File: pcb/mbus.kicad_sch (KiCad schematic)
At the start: 25 parts, among them Q2 BC846, Q3 BSS84, Q4 BC846, U3 MC33072, U4 LM4040DBZ-5

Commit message: * Work in progress
  - Add generate script
  - Add switch model
  - Start routing
  - Tidy schematic
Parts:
- added R31: 20K, Resistor_SMD:R_0402_1005Metric, symbol Device:R
- added R32: 1K, Resistor_SMD:R_0402_1005Metric, symbol Device:R
- C3: Voltage (none) -> 50V
- R9: MPN (none) -> ERJ-P06J101V; Manufacturer (none) -> Panasonic; Mouser (none) -> 667-ERJ-P06J101V; Power (none) -> 0.5W
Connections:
- net GND: now also R32.2
- net DIFF_5X renamed DIFF_5V
- net DIFF_5V: now also R31.1
- new net MBUS_OC: R31.2, R32.1
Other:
- note added: "(V > 5) saturates at 0V"
- note removed: "(V > 5) > pull low"
- note removed: "Rate for 30 mA (~90 mW)"
- note removed: "Reduce common mode voltage range to (V_{CC} - 2V7)."
- title: MBUS Master Prototype -> emonHP
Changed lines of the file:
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@@
   (paper "A4")
   (title_block
-    (title "MBUS Master Prototype")
-    (date "2024-06-26")
+    (title "emonHP")
+    (date "2024-07-02")
     (rev "0")
     (company "Tilt Ltd / OpenEnergyMonitor")
@@
   (junction (at 140.97 101.6) (diameter 0) (color 0 0 0 0)
   )
-  (junction (at 161.29 99.06) (diameter 0) (color 0 0 0 0)
-  )
   (junction (at 116.84 92.71) (diameter 0) (color 0 0 0 0)
   )
+  (junction (at 220.98 46.99) (diameter 0) (color 0 0 0 0)
+  )
   (junction (at 181.61 63.5) (diameter 0) (color 0 0 0 0)
   )
@@
     (stroke (width 0) (type default))
   )
+  (wire (pts (xy 220.98 44.45) (xy 220.98 46.99))
+    (stroke (width 0) (type default))
+  )
   (wire (pts (xy 135.89 96.52) (xy 135.89 107.95))
     (stroke (width 0) (type default))
@@
     (stroke (width 0) (type default))
   )
+  (wire (pts (xy 220.98 57.15) (xy 220.98 59.69))
+    (stroke (width 0) (type default))
+  )
   (wire (pts (xy 161.29 119.38) (xy 161.29 133.35))
     (stroke (width 0) (type default))
@@
     (stroke (width 0) (type default))
   )
-  (wire (pts (xy 161.29 99.06) (xy 171.45 99.06))
-    (stroke (width 0) (type default))
-  )
   (wire (pts (xy 54.61 57.15) (xy 68.58 57.15))
     (stroke (width 0) (type default))
@@
     (stroke (width 0) (type default))
   )
+  (wire (pts (xy 220.98 34.29) (xy 220.98 36.83))
+    (stroke (width 0) (type default))
+  )
   (wire (pts (xy 218.44 95.25) (xy 218.44 97.79))
     (stroke (width 0) (type default))
@@
     (stroke (width 0) (type default))
   )
+  (wire (pts (xy 220.98 46.99) (xy 220.98 49.53))
+    (stroke (width 0) (type default))
+  )
   (wire (pts (xy 22.86 80.01) (xy 34.29 80.01))
     (stroke (width 0) (type default))
@@
     (stroke (width 0) (type default))
   )
+  (wire (pts (xy 220.98 46.99) (xy 233.68 46.99))
+    (stroke (width 0) (type default))
+  )
   (wire (pts (xy 120.65 92.71) (xy 116.84 92.71))
     (stroke (width 0) (type default))
@@
     (stroke (width 0) (type default))
   )
-  (text "Rate for 30 mA (~90 mW)" (at 73.66 100.33 0)
-    (effects (font (size 1.27 1.27)) (justify left bottom))
-  )
-  (text "Reduce common mode voltage\nrange to (V_{CC} - 2V7)."
-    (at 73.66 86.36 0)
-    (effects (font (size 1.27 1.27)) (justify left bottom))
+  (text_box "When the voltage through the shunt resistor is >5 V, this indicates a short on MBUS, so shut down."
+    (at 237.49 30.48 0) (size 29.21 10.16)
+    (stroke (width 0) (type default))
+    (fill (type none))
+    (effects (font (size 1.27 1.27)) (justify left top))
+  )
+  (text_box "Reduce common mode voltage\nrange to (V_{CC} - 2V7)."
+    (at 68.58 81.28 0) (size 33.02 6.35)
+    (stroke (width 0) (type default))
+    (fill (type none))
+    (effects (font (size 1.27 1.27)) (justify left top))
   )
   (text "Gain: 5" (at 134.62 92.71 0)
     (effects (font (size 1.27 1.27)) (justify left bottom))
   )
-  (text "(V > 5) > pull low" (at 193.04 123.19 0)
+  (text "(V > 5) saturates at 0V" (at 184.15 124.46 0)
     (effects (font (size 1.27 1.27)) (justify left bottom))
   )
@@
     (effects (font (size 1.27 1.27)) (justify right bottom))
   )
-  (label "V_{Z}" (at 132.08 76.2 180) (fields_autoplaced)
-    (effects (font (size 1.27 1.27)) (justify right bottom))
-  )
   (label "MBUS_A" (at 109.22 132.08 0) (fields_autoplaced)
     (effects (font (size 1.27 1.27)) (justify left bottom))
   )
+  (label "DIFF_5V" (at 220.98 34.29 0) (fields_autoplaced)
+    (effects (font (size 1.27 1.27)) (justify left bottom))
+  )
   (label "36V" (at 54.61 57.15 0) (fields_autoplaced)
     (effects (font (size 1.27 1.27)) (justify left bottom))
@@
     (effects (font (size 1.27 1.27)) (justify right bottom))
   )
+  (label "DIFF_5V" (at 161.29 99.06 0) (fields_autoplaced)
+    (effects (font (size 1.27 1.27)) (justify left bottom))
+  )
   (hierarchical_label "MBUS_A" (shape output) (at 100.33 132.08 180) (fields_autoplaced)
     (effects (font (size 1.27 1.27)) (justify right))
@@
     (effects (font (size 1.27 1.27)) (justify left))
   )
-  (hierarchical_label "DIFF_5X" (shape output) (at 171.45 99.06 0) (fields_autoplaced)
+  (hierarchical_label "MBUS_OC" (shape passive) (at 233.68 46.99 0) (fields_autoplaced)
     (effects (font (size 1.27 1.27)) (justify left))
   )
@@
     )
   )
+  (symbol (lib_id "power:GND") (at 220.98 59.69 0) (unit 1)
+    (in_bom yes) (on_board yes) (dnp no) (fields_autoplaced)
+    (property "Reference" "#PWR052" (at 220.98 66.04 0)
+      (effects (font (size 1.27 1.27)) hide)
+    )
+    (property "Value" "GND" (at 220.98 64.77 0)
+      (effects (font (size 1.27 1.27)))
+    )
+    (property "Footprint" "" (at 220.98 59.69 0)
+      (effects (font (size 1.27 1.27)) hide)
+    )
+    (property "Datasheet" "" (at 220.98 59.69 0)
+      (effects (font (size 1.27 1.27)) hide)
+    )
+    (pin "1")
+    (instances
+      (project "emonHP"
+        (path "/afefbb79-c2cc-4097-b792-3e37a295b6e5"
+          (reference "#PWR052") (unit 1)
+        )
+        (path "/afefbb79-c2cc-4097-b792-3e37a295b6e5/47d3f211-4a48-4ab2-adbe-56046b34137e"
+          (reference "#PWR052") (unit 1)
+        )
+      )
+    )
+  )
   (symbol (lib_id "Device:R") (at 34.29 71.12 180) (unit 1)
     (in_bom yes) (on_board yes) (dnp no) (fields_autoplaced)
@@
   )
   (symbol (lib_id "Device:C") (at 194.31 71.12 0) (mirror y) (unit 1)
-    (in_bom yes) (on_board yes) (dnp no) (fields_autoplaced)
+    (in_bom yes) (on_board yes) (dnp no)
     (property "Reference" "C3" (at 190.5 70.485 0)
       (effects (font (size 1.27 1.27)) (justify left))
@@
       (effects (font (size 1.27 1.27)) hide)
     )
+    (property "Voltage" "50V" (at 189.23 76.2 0)
+      (effects (font (size 1.27 1.27)))
+    )
     (pin "1")
     (pin "2")
@@
   )
   (symbol (lib_id "Device:R") (at 116.84 99.06 0) (mirror y) (unit 1)
-    (in_bom yes) (on_board yes) (dnp no) (fields_autoplaced)
+    (in_bom yes) (on_board yes) (dnp no)
     (property "Reference" "R9" (at 114.3 98.425 0)
       (effects (font (size 1.27 1.27)) (justify left))
@@
       (effects (font (size 1.27 1.27)) hide)
     )
+    (property "Manufacturer" "Panasonic" (at 116.84 99.06 0)
+      (effects (font (size 1.27 1.27)) hide)
+    )
+    (property "MPN" "ERJ-P06J101V" (at 116.84 99.06 0)
+      (effects (font (size 1.27 1.27)) hide)
+    )
+    (property "Mouser" "667-ERJ-P06J101V" (at 116.84 99.06 0)
+      (effects (font (size 1.27 1.27)) hide)
+    )
+    (property "Power" "0.5W" (at 111.76 102.87 0)
+      (effects (font (size 1.27 1.27)))
+    )
     (pin "1")
     (pin "2")
@@
         )
       )
+    )
+  )
+  (symbol (lib_id "Device:R") (at 220.98 40.64 0) (unit 1)
+    (in_bom yes) (on_board yes) (dnp no) (fields_autoplaced)
+    (property "Reference" "R31" (at 223.52 40.005 0)
+      (effects (font (size 1.27 1.27)) (justify left))
+    )
+    (property "Value" "20K" (at 223.52 42.545 0)
+      (effects (font (size 1.27 1.27)) (justify left))
+    )
+    (property "Footprint" "Resistor_SMD:R_0402_1005Metric" (at 219.202 40.64 90)
+      (effects (font (size 1.27 1.27)) hide)
+    )
+    (property "Datasheet" "~" (at 220.98 40.64 0)
+      (effects (font (size 1.27 1.27)) hide)
+    )
+    (pin "1")
+    (pin "2")
+    (instances
+      (project "emonHP"
+        (path "/afefbb79-c2cc-4097-b792-3e37a295b6e5"
+          (reference "R31") (unit 1)
+        )
+        (path "/afefbb79-c2cc-4097-b792-3e37a295b6e5/47d3f211-4a48-4ab2-adbe-56046b34137e"
+          (reference "R31") (unit 1)
+        )
+      )
+    )
+  )
+  (symbol (lib_id "Device:R") (at 220.98 53.34 0) (unit 1)
+    (in_bom yes) (on_board yes) (dnp no) (fields_autoplaced)
+    (property "Reference" "R32" (at 223.52 52.705 0)
+      (effects (font (size 1.27 1.27)) (justify left))
+    )
+    (property "Value" "1K" (at 223.52 55.245 0)
+      (effects (font (size 1.27 1.27)) (justify left))
+    )
+    (property "Footprint" "Resistor_SMD:R_0402_1005Metric" (at 219.202 53.34 90)
+      (effects (font (size 1.27 1.27)) hide)
+    )
+    (property "Datasheet" "~" (at 220.98 53.34 0)
+      (effects (font (size 1.27 1.27)) hide)
+    )
+    (pin "1")
+    (pin "2")
+    (instances
+      (project "emonHP"
+        (path "/afefbb79-c2cc-4097-b792-3e37a295b6e5"
+          (reference "R32") (unit 1)
+        )
+        (path "/afefbb79-c2cc-4097-b792-3e37a295b6e5/47d3f211-4a48-4ab2-adbe-56046b34137e"
+          (reference "R32") (unit 1)
+        )
+      )

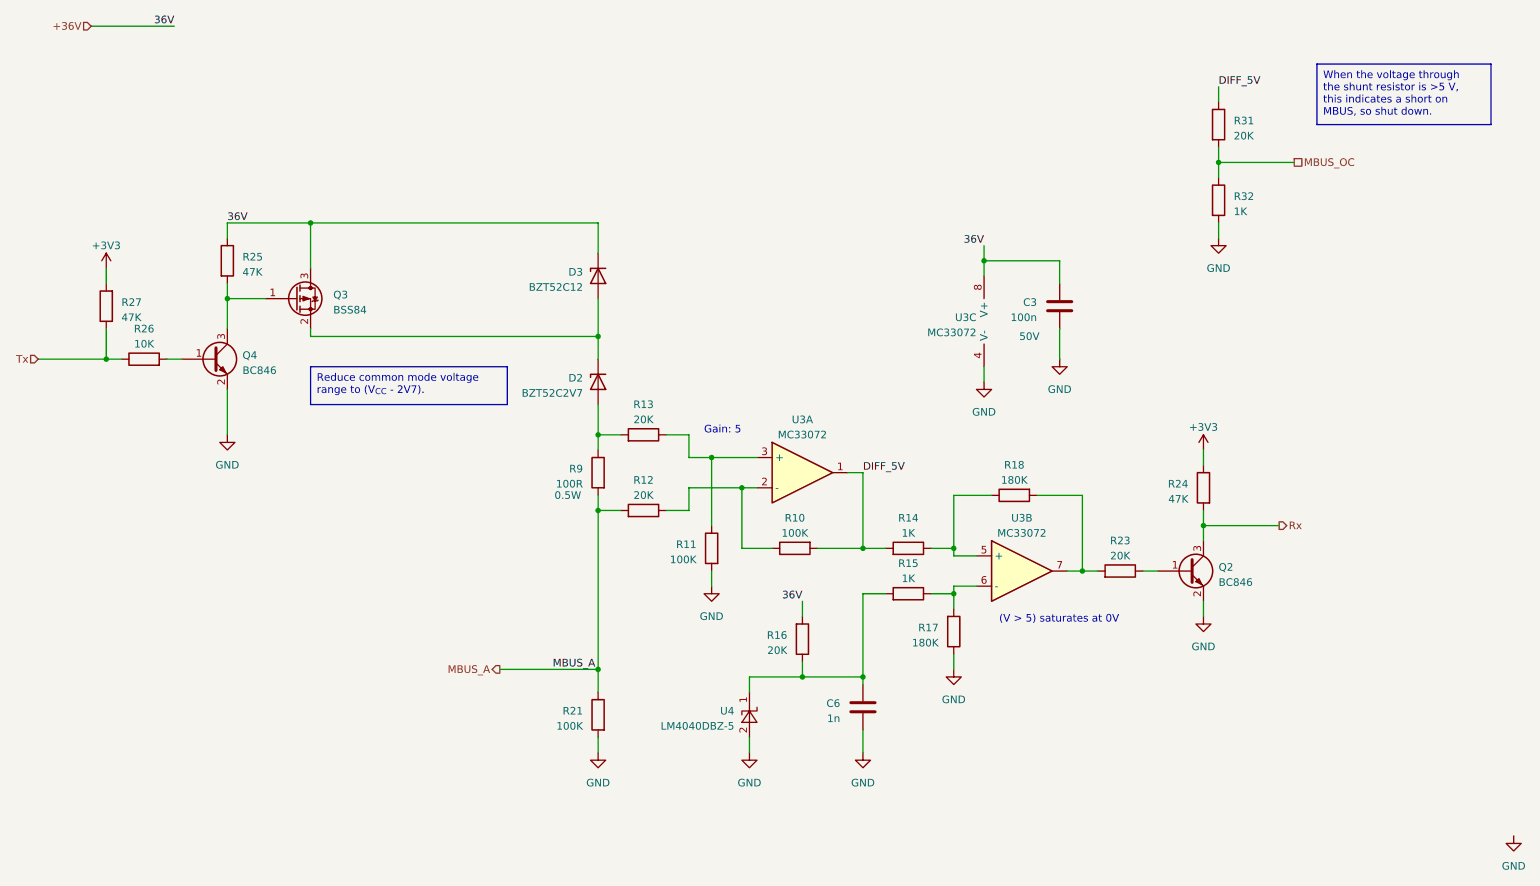
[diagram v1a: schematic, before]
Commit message: * [0.1-dev] Voltage good
  - Add 36V voltage good detection
  - Add all 3D models
  - Correct footprint for front LED
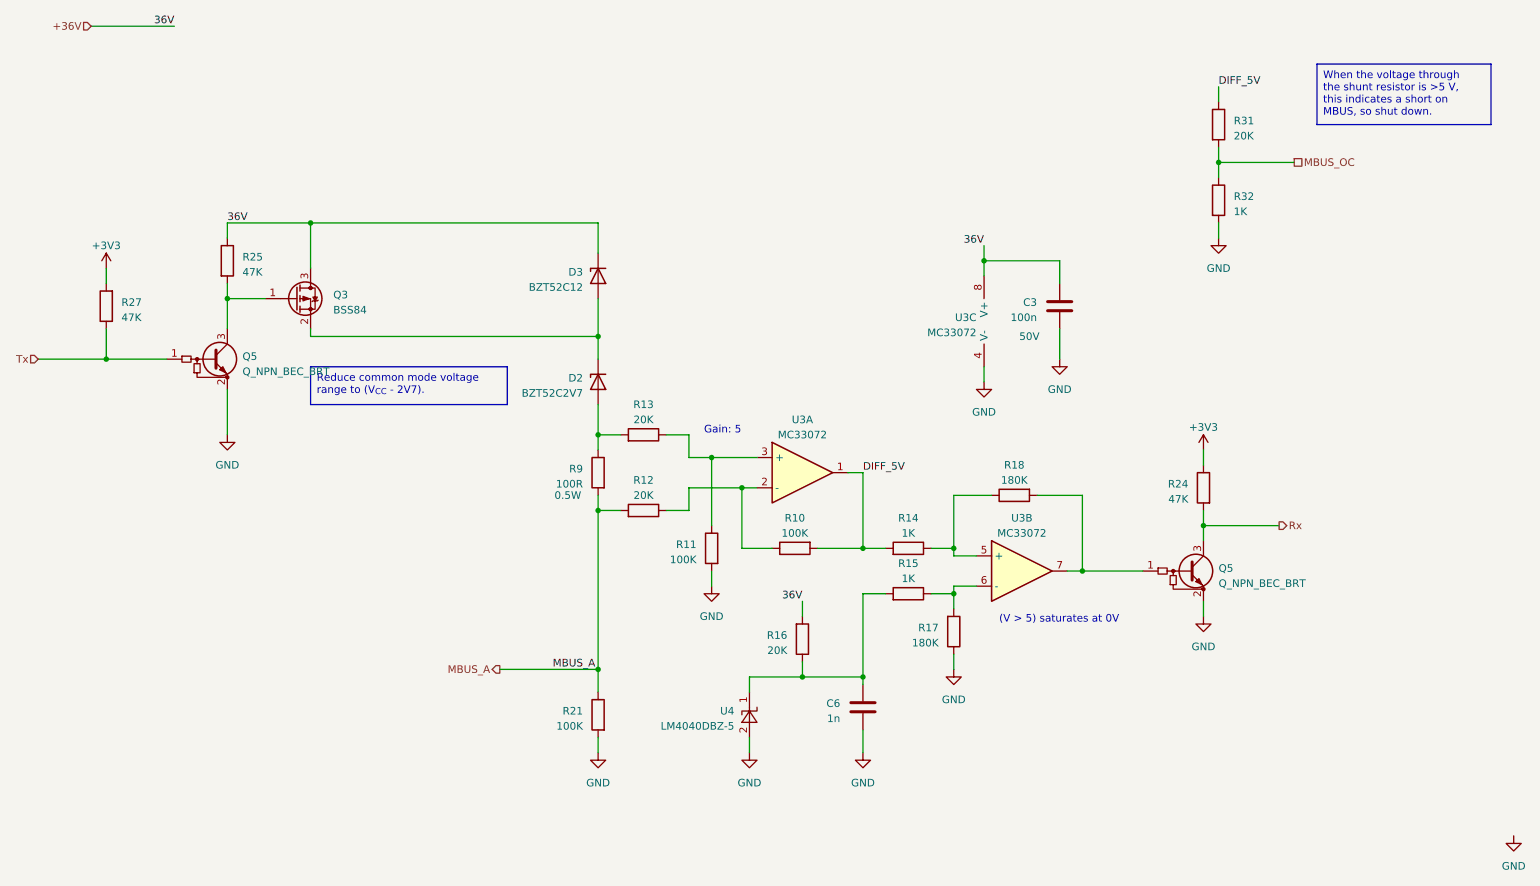
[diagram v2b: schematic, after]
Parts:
- removed Q2, Q4: BC846, Package_TO_SOT_SMD:SOT-23, symbol Transistor_BJT:BC846
- removed R23: 20K, Resistor_SMD:R_0402_1005Metric, symbol Device:R
- removed R26: 10K, Resistor_SMD:R_0402_1005Metric, symbol Device:R
- added Q5 (x2): Q_NPN_BEC_BRT, Package_TO_SOT_SMD:SOT-23, symbol Device:Q_NPN_BEC_BRT
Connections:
- net GND: now also Q5.2 (E), Q5.2 (E)
- net Rx: now also Q5.3 (C)
- net Tx: now also Q5.1 (B)
- net at Q3.1 (G), R25.2: now also Q5.3 (C)
- net at R18.2, U3.7: now also Q5.1 (B)
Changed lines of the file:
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@@
     (stroke (width 0) (type default))
   )
-  (wire (pts (xy 36.83 80.01) (xy 34.29 80.01))
+  (wire (pts (xy 34.29 80.01) (xy 44.45 80.01))
     (stroke (width 0) (type default))
   )
@@
     (stroke (width 0) (type default))
   )
-  (wire (pts (xy 44.45 80.01) (xy 46.99 80.01))
-    (stroke (width 0) (type default))
-  )
   (wire (pts (xy 231.14 107.95) (xy 218.44 107.95))
     (stroke (width 0) (type default))
@@
     (stroke (width 0) (type default))
   )
-  (wire (pts (xy 210.82 115.57) (xy 208.28 115.57))
-    (stroke (width 0) (type default))
-  )
   (wire (pts (xy 116.84 92.71) (xy 116.84 95.25))
     (stroke (width 0) (type default))
@@
     (stroke (width 0) (type default))
   )
-  (wire (pts (xy 200.66 115.57) (xy 198.12 115.57))
+  (wire (pts (xy 198.12 115.57) (xy 208.28 115.57))
     (stroke (width 0) (type default))
   )
@@
     )
   )
+  (symbol (lib_id "Device:Q_NPN_BEC_BRT") (at 53.34 80.01 0) (unit 1)
+    (in_bom yes) (on_board yes) (dnp no) (fields_autoplaced)
+    (property "Reference" "Q5" (at 57.15 79.5528 0)
+      (effects (font (size 1.27 1.27)) (justify left))
+    )
+    (property "Value" "Q_NPN_BEC_BRT" (at 57.15 82.0928 0)
+      (effects (font (size 1.27 1.27)) (justify left))
+    )
+    (property "Footprint" "Package_TO_SOT_SMD:SOT-23" (at 53.34 80.01 0)
+      (effects (font (size 1.27 1.27)) hide)
+    )
+    (property "Datasheet" "~" (at 53.34 80.01 0)
+      (effects (font (size 1.27 1.27)) hide)
+    )
+    (pin "1")
+    (pin "2")
+    (pin "3")
+    (instances
+      (project "emonHP"
+        (path "/afefbb79-c2cc-4097-b792-3e37a295b6e5"
+          (reference "Q5") (unit 1)
+        )
+        (path "/afefbb79-c2cc-4097-b792-3e37a295b6e5/47d3f211-4a48-4ab2-adbe-56046b34137e"
+          (reference "Q1") (unit 1)
+        )
+      )
+    )
+  )
   (symbol (lib_id "power:GND") (at 142.24 146.05 0) (mirror y) (unit 1)
     (in_bom yes) (on_board yes) (dnp no) (fields_autoplaced)
@@
         (path "/afefbb79-c2cc-4097-b792-3e37a295b6e5/47d3f211-4a48-4ab2-adbe-56046b34137e"
           (reference "R10") (unit 1)
-        )
-      )
-    )
-  )
-  (symbol (lib_id "Transistor_BJT:BC846") (at 52.07 80.01 0) (unit 1)
-    (in_bom yes) (on_board yes) (dnp no) (fields_autoplaced)
-    (property "Reference" "Q4" (at 57.15 79.375 0)
-      (effects (font (size 1.27 1.27)) (justify left))
-    )
-    (property "Value" "BC846" (at 57.15 81.915 0)
-      (effects (font (size 1.27 1.27)) (justify left))
-    )
-    (property "Footprint" "Package_TO_SOT_SMD:SOT-23" (at 57.15 81.915 0)
-      (effects (font (size 1.27 1.27) italic) (justify left) hide)
-    )
-    (property "Datasheet" "https://assets.nexperia.com/documents/data-sheet/BC846_SER.pdf" (at 52.07 80.01 0)
-      (effects (font (size 1.27 1.27)) (justify left) hide)
-    )
-    (pin "1")
-    (pin "2")
-    (pin "3")
-    (instances
-      (project "mbus-reader-proto"
-        (path "/36d146b0-f348-4341-a935-471af0e684a6"
-          (reference "Q4") (unit 1)
-        )
-      )
-      (project "emonHP"
-        (path "/afefbb79-c2cc-4097-b792-3e37a295b6e5/47d3f211-4a48-4ab2-adbe-56046b34137e"
-          (reference "Q1") (unit 1)
         )
       )
@@
     )
   )
-  (symbol (lib_id "Device:R") (at 204.47 115.57 270) (mirror x) (unit 1)
-    (in_bom yes) (on_board yes) (dnp no) (fields_autoplaced)
-    (property "Reference" "R23" (at 204.47 110.49 90)
-      (effects (font (size 1.27 1.27)))
-    )
-    (property "Value" "20K" (at 204.47 113.03 90)
-      (effects (font (size 1.27 1.27)))
-    )
-    (property "Footprint" "Resistor_SMD:R_0402_1005Metric" (at 204.47 117.348 90)
-      (effects (font (size 1.27 1.27)) hide)
-    )
-    (property "Datasheet" "~" (at 204.47 115.57 0)
-      (effects (font (size 1.27 1.27)) hide)
-    )
-    (pin "1")
-    (pin "2")
-    (instances
-      (project "mbus-reader-proto"
-        (path "/36d146b0-f348-4341-a935-471af0e684a6"
-          (reference "R23") (unit 1)
-        )
-      )
-      (project "emonHP"
-        (path "/afefbb79-c2cc-4097-b792-3e37a295b6e5/47d3f211-4a48-4ab2-adbe-56046b34137e"
-          (reference "R25") (unit 1)
-        )
-      )
-    )
-  )
-  (symbol (lib_id "Device:R") (at 40.64 80.01 90) (unit 1)
-    (in_bom yes) (on_board yes) (dnp no) (fields_autoplaced)
-    (property "Reference" "R26" (at 40.64 74.93 90)
-      (effects (font (size 1.27 1.27)))
-    )
-    (property "Value" "10K" (at 40.64 77.47 90)
-      (effects (font (size 1.27 1.27)))
-    )
-    (property "Footprint" "Resistor_SMD:R_0402_1005Metric" (at 40.64 81.788 90)
-      (effects (font (size 1.27 1.27)) hide)
-    )
-    (property "Datasheet" "~" (at 40.64 80.01 0)
-      (effects (font (size 1.27 1.27)) hide)
-    )
-    (pin "1")
-    (pin "2")
-    (instances
-      (project "mbus-reader-proto"
-        (path "/36d146b0-f348-4341-a935-471af0e684a6"
-          (reference "R26") (unit 1)
-        )
-      )
-      (project "emonHP"
-        (path "/afefbb79-c2cc-4097-b792-3e37a295b6e5/47d3f211-4a48-4ab2-adbe-56046b34137e"
-          (reference "R7") (unit 1)
-        )
-      )
-    )
-  )
   (symbol (lib_id "Diode:BZT52Bxx") (at 116.84 66.04 90) (mirror x) (unit 1)
     (in_bom yes) (on_board yes) (dnp no) (fields_autoplaced)
@@
         (path "/afefbb79-c2cc-4097-b792-3e37a295b6e5/47d3f211-4a48-4ab2-adbe-56046b34137e"
           (reference "D2") (unit 1)
+        )
+      )
+    )
+  )
+  (symbol (lib_id "Device:Q_NPN_BEC_BRT") (at 217.17 115.57 0) (unit 1)
+    (in_bom yes) (on_board yes) (dnp no) (fields_autoplaced)
+    (property "Reference" "Q5" (at 220.98 115.1128 0)
+      (effects (font (size 1.27 1.27)) (justify left))
+    )
+    (property "Value" "Q_NPN_BEC_BRT" (at 220.98 117.6528 0)
+      (effects (font (size 1.27 1.27)) (justify left))
+    )
+    (property "Footprint" "Package_TO_SOT_SMD:SOT-23" (at 217.17 115.57 0)
+      (effects (font (size 1.27 1.27)) hide)
+    )
+    (property "Datasheet" "~" (at 217.17 115.57 0)
+      (effects (font (size 1.27 1.27)) hide)
+    )
+    (pin "1")
+    (pin "2")
+    (pin "3")
+    (instances
+      (project "emonHP"
+        (path "/afefbb79-c2cc-4097-b792-3e37a295b6e5"
+          (reference "Q5") (unit 1)
+        )
+        (path "/afefbb79-c2cc-4097-b792-3e37a295b6e5/47d3f211-4a48-4ab2-adbe-56046b34137e"
+          (reference "Q4") (unit 1)
         )
       )
@@
         )
       )
-    )
-  )
-  (symbol (lib_id "Transistor_BJT:BC846") (at 215.9 115.57 0) (unit 1)
-    (in_bom yes) (on_board yes) (dnp no) (fields_autoplaced)
-    (property "Reference" "Q2" (at 220.98 114.935 0)
-      (effects (font (size 1.27 1.27)) (justify left))
-    )
-    (property "Value" "BC846" (at 220.98 117.475 0)
-      (effects (font (size 1.27 1.27)) (justify left))
-    )
-    (property "Footprint" "Package_TO_SOT_SMD:SOT-23" (at 220.98 117.475 0)
-      (effects (font (size 1.27 1.27) italic) (justify left) hide)
-    )
-    (property "Datasheet" "https://assets.nexperia.com/documents/data-sheet/BC846_SER.pdf" (at 215.9 115.57 0)
-      (effects (font (size 1.27 1.27)) (justify left) hide)
-    )
-    (pin "1")
-    (pin "2")
-    (pin "3")
-    (instances
-      (project "mbus-reader-proto"
-        (path "/36d146b0-f348-4341-a935-471af0e684a6"
-          (reference "Q2") (unit 1)
-        )
-      )
-      (project "emonHP"
-        (path "/afefbb79-c2cc-4097-b792-3e37a295b6e5/47d3f211-4a48-4ab2-adbe-56046b34137e"
-          (reference "Q3") (unit 1)
-        )
-      )
